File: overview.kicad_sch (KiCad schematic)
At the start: 2 parts, among them U1 SN74LVC8T245, U2 SN75160BDW

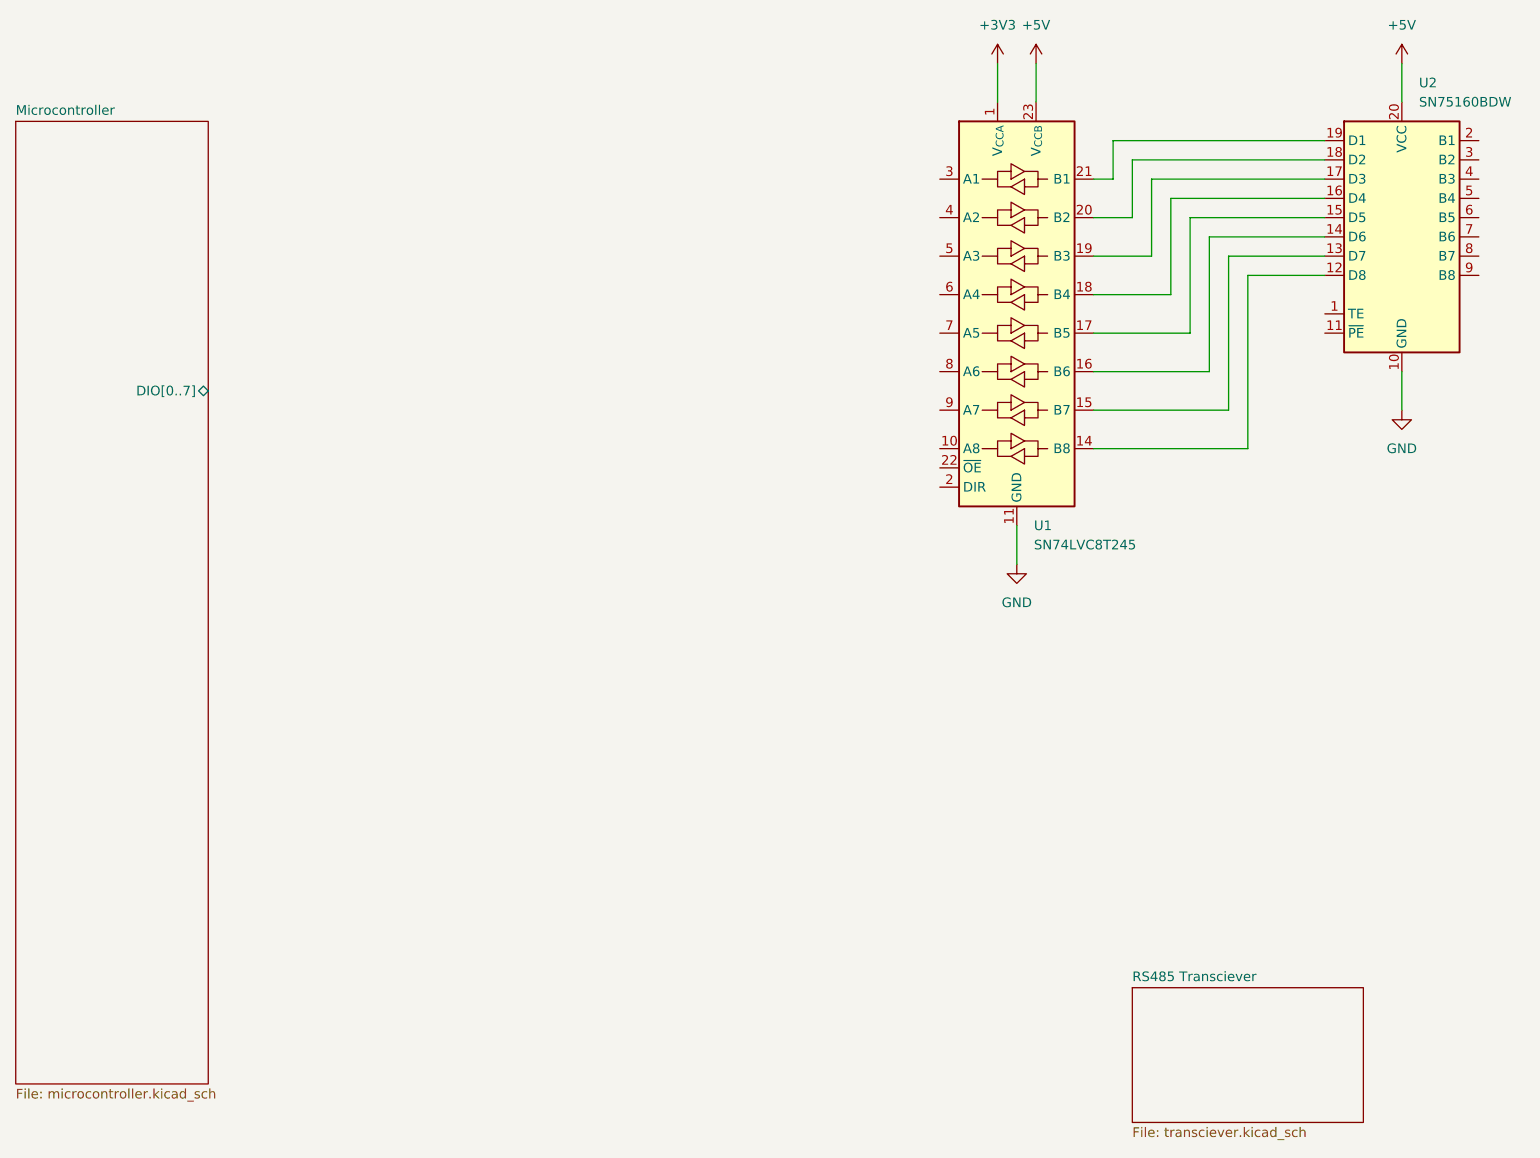
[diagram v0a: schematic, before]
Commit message: Add connectors and GPIB sub-sheets
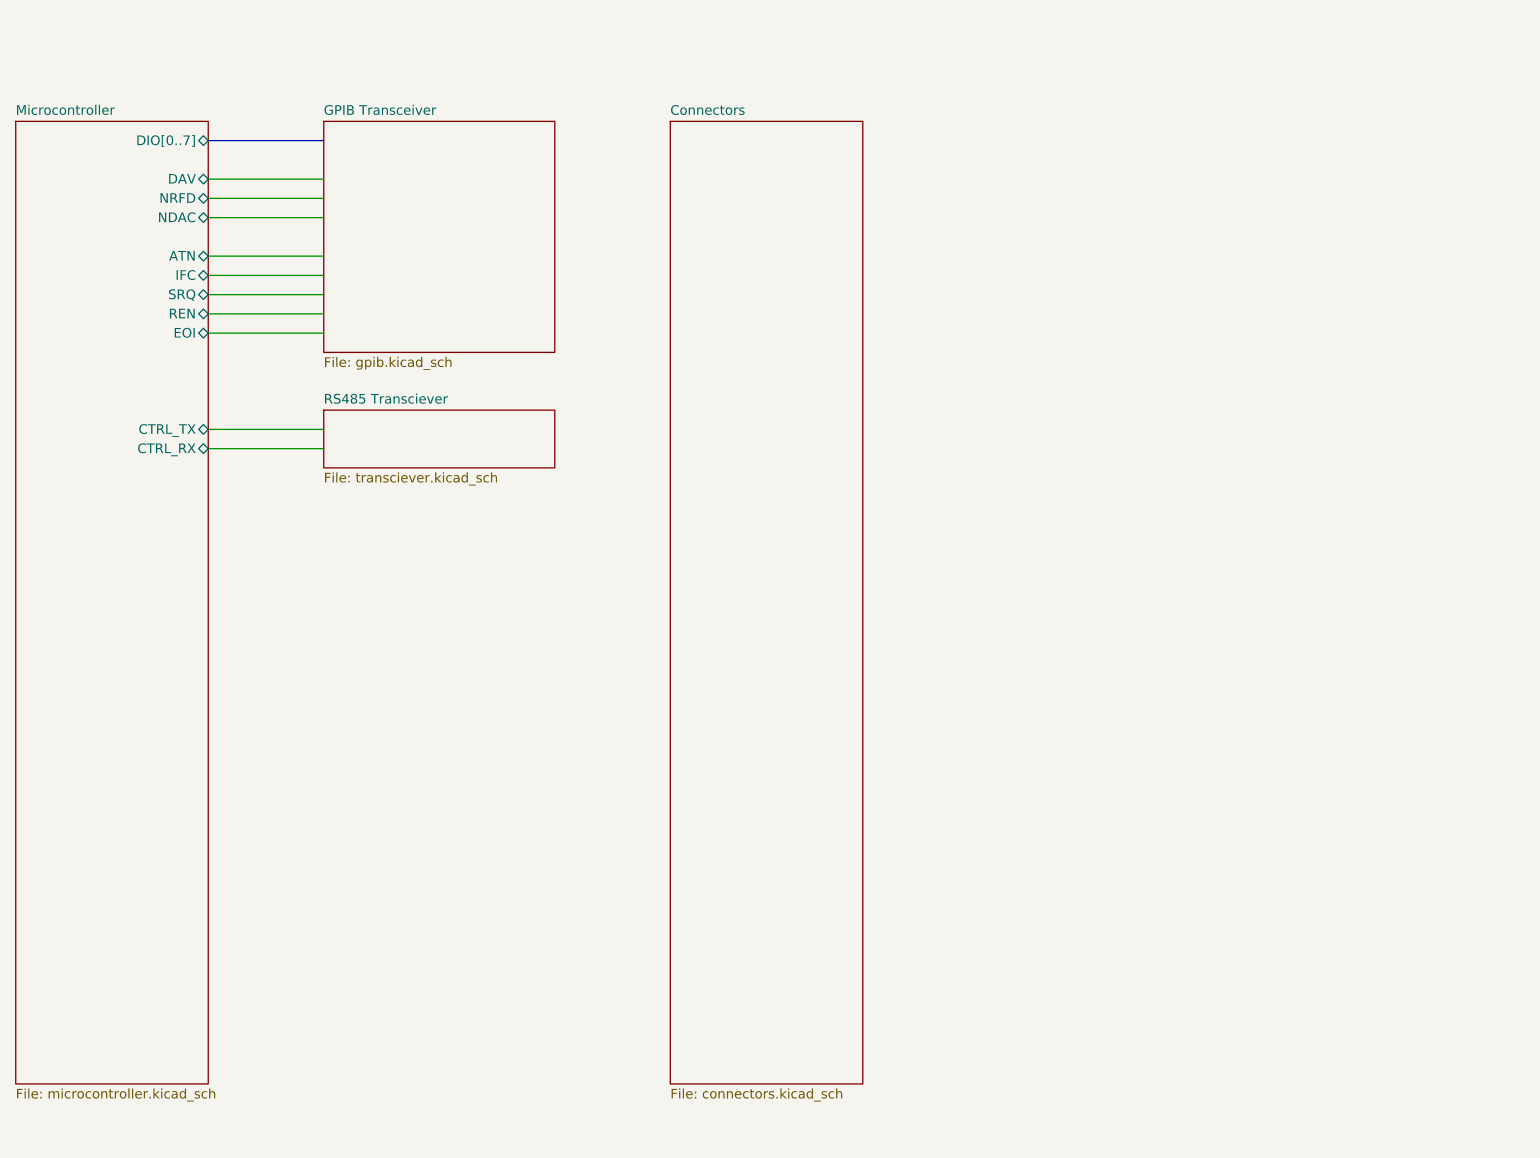
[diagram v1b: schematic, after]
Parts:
- removed U1: SN74LVC8T245, symbol Logic_LevelTranslator:SN74LVC8T245
- removed U2: SN75160BDW, Package_SO:SOIC-20W_7.5x12.8mm_P1.27mm, symbol Interface:SN75160BDW
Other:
- added sheet Connectors (connectors.kicad_sch)
- added sheet GPIB Transceiver (gpib.kicad_sch)
- sheet Microcontroller ports: added ATN, CTRL_RX, CTRL_TX, DAV, EOI, IFC, NDAC, NRFD, REN, SRQ; removed none

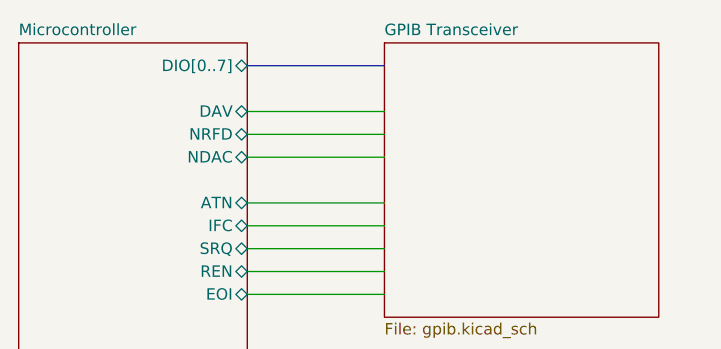
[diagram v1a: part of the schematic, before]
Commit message: Remove GPIB transcievers. Targeting modern replacements
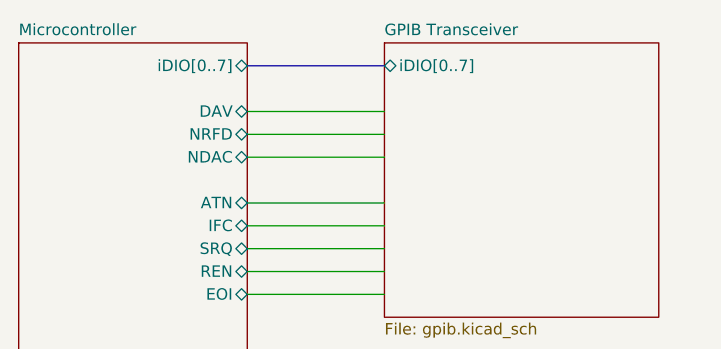
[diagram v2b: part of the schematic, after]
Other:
- sheet GPIB Transceiver ports: added iDIO[0..7]; removed none
- sheet Microcontroller ports: added iDIO[0..7]; removed DIO[0..7]
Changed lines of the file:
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@@
+			)
+		)
+		(pin "iDIO[0..7]" bidirectional
+			(at 167.64 71.12 180)
+			(effects
+				(font
+					(size 1.27 1.27)
+				)
+				(justify left)
 			)
 		)
@@
 				)
 				(justify left top)
-			)
-		)
-		(pin "DIO[0..7]" bidirectional
-			(at 152.4 71.12 0)
-			(effects
-				(font
-					(size 1.27 1.27)
-				)
-				(justify right)
 			)
 		)
@@
 			(effects
 				(font
+					(size 1.27 1.27)
+				)
+				(justify right)
+			)
+		)
+		(pin "iDIO[0..7]" bidirectional
+			(at 152.4 71.12 0)
+			(effects
+				(font

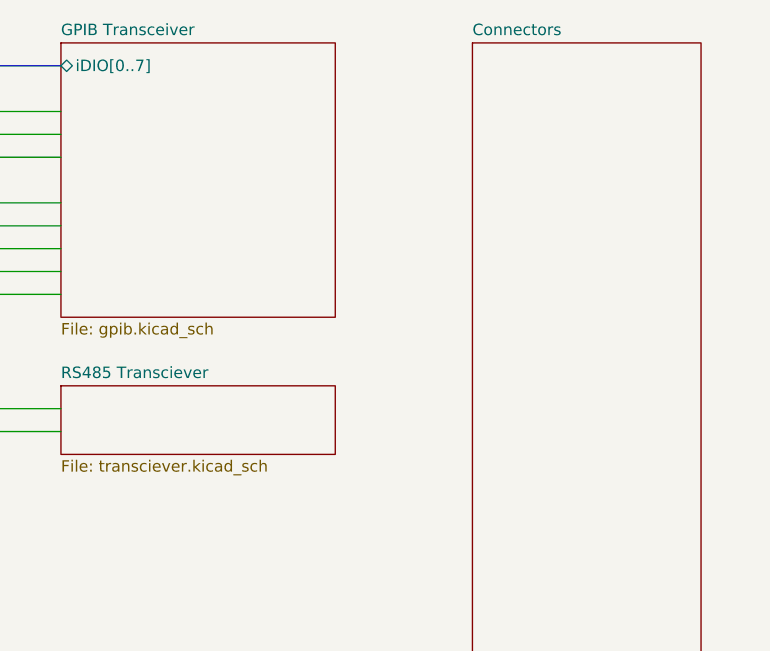
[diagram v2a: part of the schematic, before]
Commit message: Link DIO nets to GPIB connector
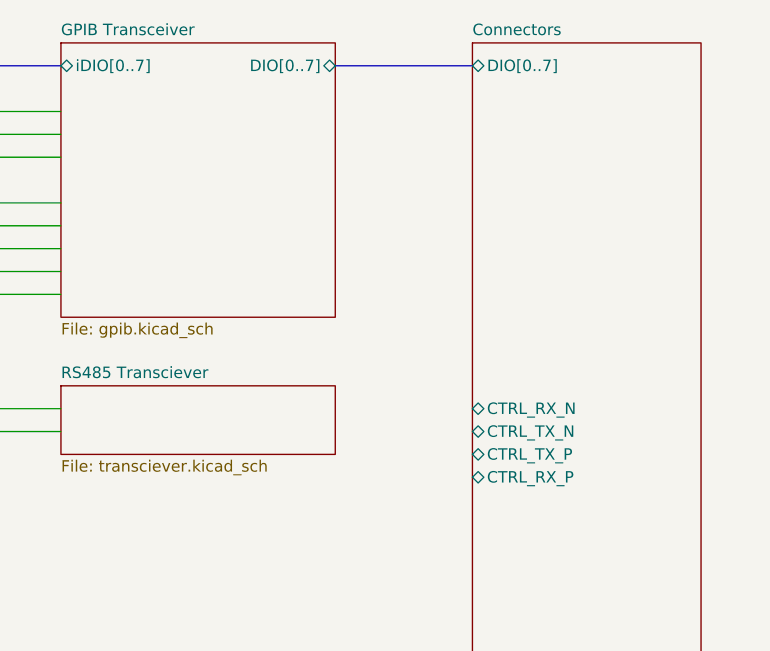
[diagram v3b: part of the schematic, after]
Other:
- sheet Connectors ports: added CTRL_RX_N, CTRL_RX_P, CTRL_TX_N, CTRL_TX_P, DIO[0..7]; removed none
- sheet GPIB Transceiver ports: added DIO[0..7]; removed none
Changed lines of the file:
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@@
+		)
+	)
+	(bus
+		(pts
+			(xy 198.12 71.12) (xy 213.36 71.12)
+		)
+		(stroke
+			(width 0)
+			(type default)
 		)
 	)
@@
 			)
 		)
+		(pin "DIO[0..7]" bidirectional
+			(at 198.12 71.12 0)
+			(effects
+				(font
+					(size 1.27 1.27)
+				)
+				(justify right)
+			)
+		)
 		(instances
 			(project "gpib_controller"
@@
 			)
 		)
+		(pin "DIO[0..7]" bidirectional
+			(at 213.36 71.12 180)
+			(effects
+				(font
+					(size 1.27 1.27)
+				)
+				(justify left)
+			)
+		)
+		(pin "CTRL_RX_N" bidirectional
+			(at 213.36 109.22 180)
+			(effects
+				(font
+					(size 1.27 1.27)
+				)
+				(justify left)
+			)
+		)
+		(pin "CTRL_TX_N" bidirectional
+			(at 213.36 111.76 180)
+			(effects
+				(font
+					(size 1.27 1.27)
+				)
+				(justify left)
+			)
+		)
+		(pin "CTRL_TX_P" bidirectional
+			(at 213.36 114.3 180)
+			(effects
+				(font
+					(size 1.27 1.27)
+				)
+				(justify left)
+			)
+		)
+		(pin "CTRL_RX_P" bidirectional
+			(at 213.36 116.84 180)
+			(effects
+				(font
+					(size 1.27 1.27)
+				)
+				(justify left)
+			)
+		)

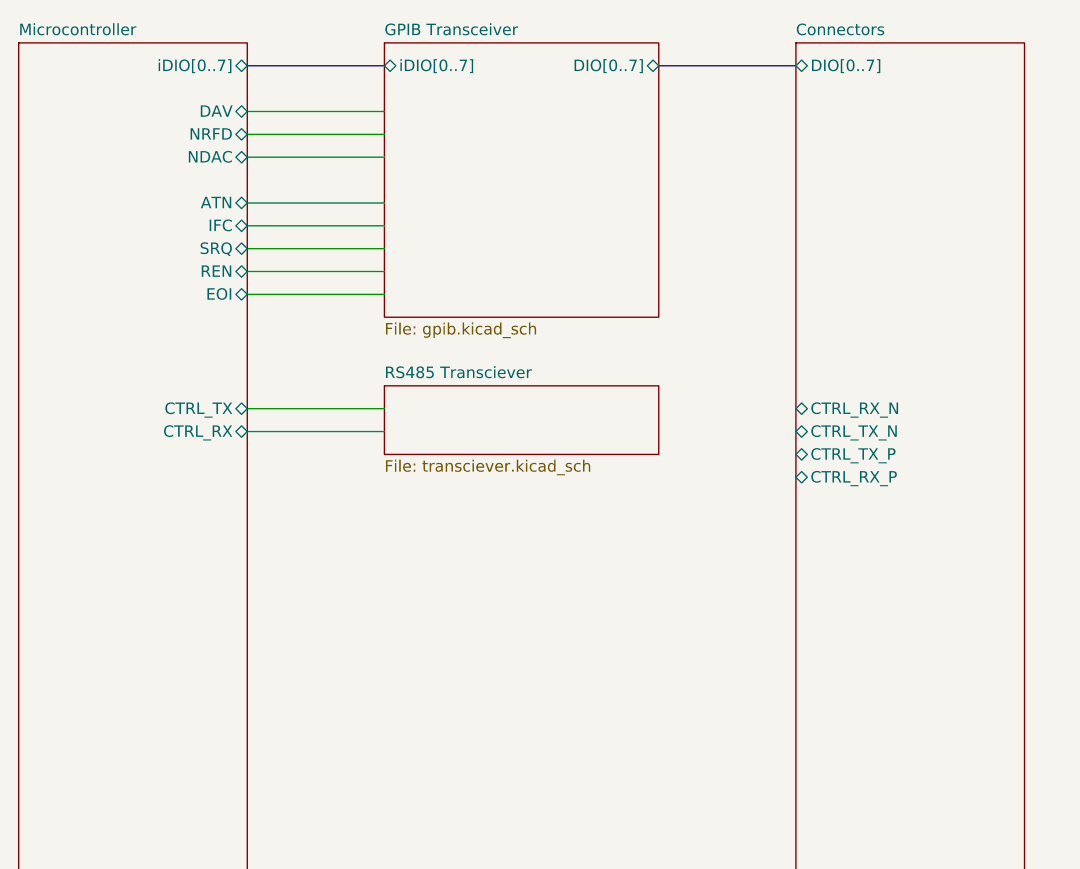
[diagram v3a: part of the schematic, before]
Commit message: Added open-drain driver for GPIB control pins
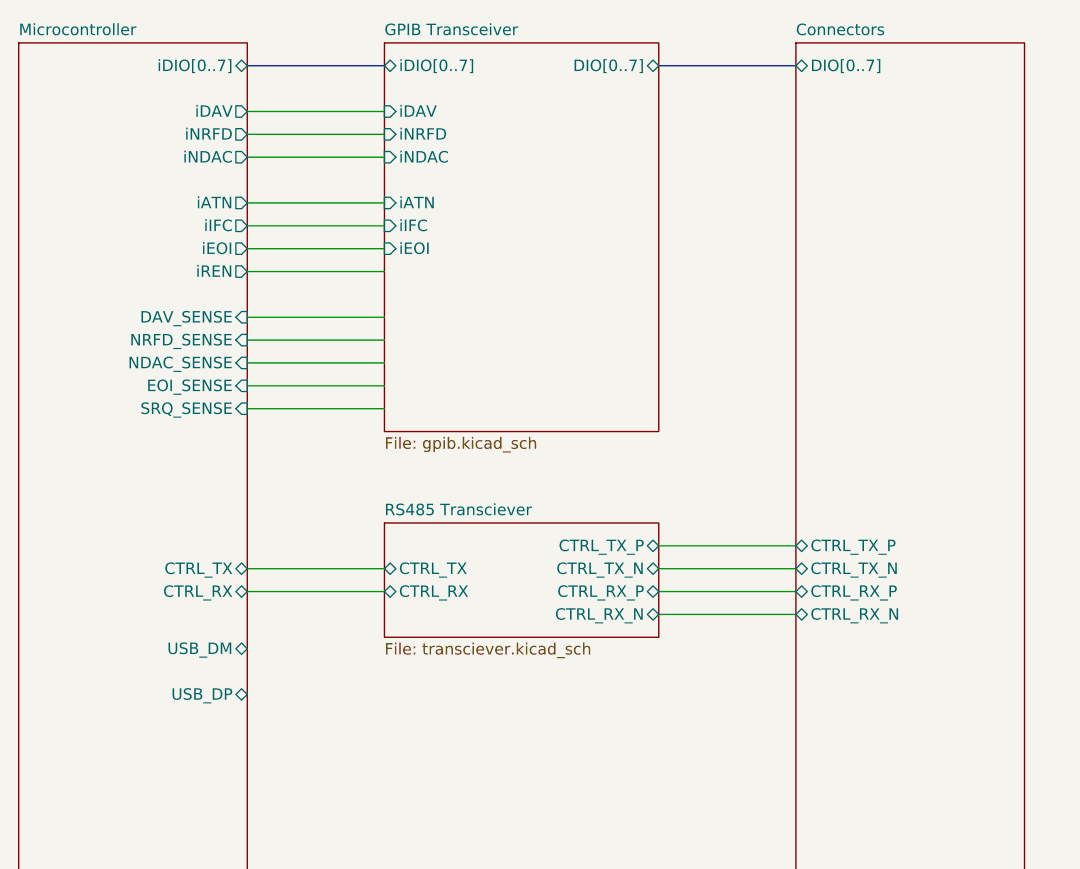
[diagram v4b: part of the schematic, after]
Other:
- sheet GPIB Transceiver ports: added iATN, iDAV, iEOI, iIFC, iNDAC, iNRFD; removed none
- sheet Microcontroller ports: added DAV_SENSE, EOI_SENSE, NDAC_SENSE, NRFD_SENSE, SRQ_SENSE, USB_DM, USB_DP, iATN, iDAV, iEOI, iIFC, iNDAC, iNRFD, iREN; removed ATN, DAV, EOI, IFC, NDAC, NRFD, REN, SRQ
- sheet RS485 Transciever ports: added CTRL_RX, CTRL_RX_N, CTRL_RX_P, CTRL_TX, CTRL_TX_N, CTRL_TX_P; removed none

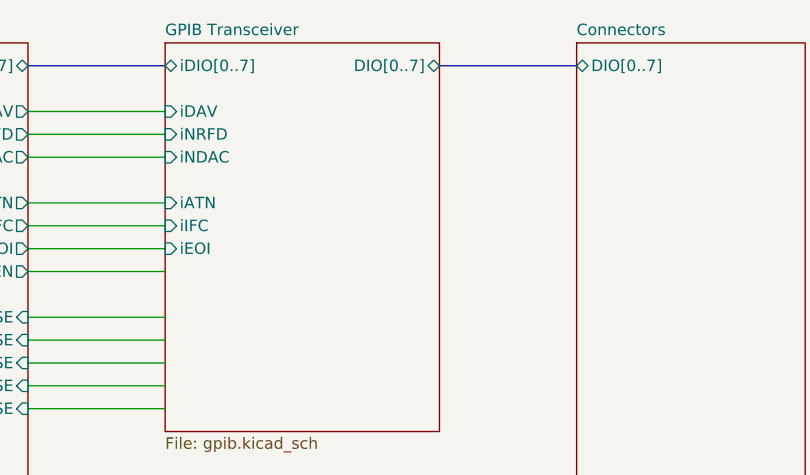
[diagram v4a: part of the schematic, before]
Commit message: Add Schmitt-Trig sense IC, connect GPIB conn nets and run jobfile
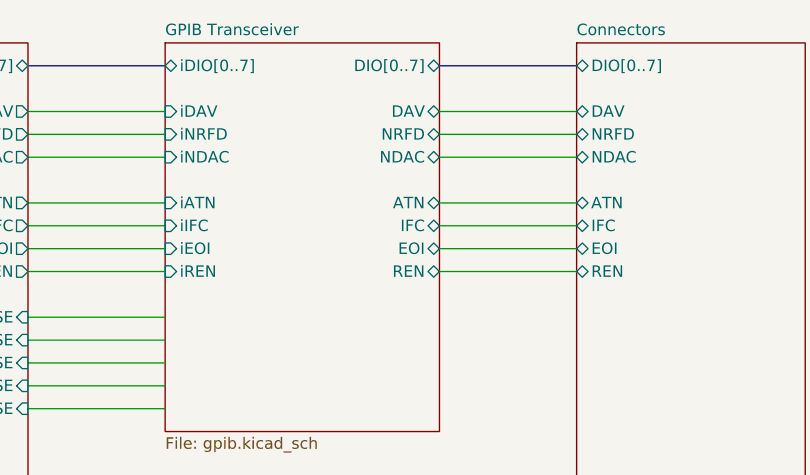
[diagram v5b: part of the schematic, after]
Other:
- sheet Connectors ports: added ATN, DAV, EOI, IFC, NDAC, NRFD, REN; removed none
- sheet GPIB Transceiver ports: added ATN, DAV, EOI, IFC, NDAC, NRFD, REN, iREN; removed none
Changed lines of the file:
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@@
+	(wire
+		(pts
+			(xy 198.12 78.74) (xy 213.36 78.74)
+		)
+		(stroke
+			(width 0)
+			(type default)
+		)
+	)
 	(wire
 		(pts
@@
 	(wire
 		(pts
+			(xy 198.12 88.9) (xy 213.36 88.9)
+		)
+		(stroke
+			(width 0)
+			(type default)
+		)
+	)
+	(wire
+		(pts
 			(xy 198.12 129.54) (xy 213.36 129.54)
 		)
@@
 	(wire
 		(pts
+			(xy 198.12 81.28) (xy 213.36 81.28)
+		)
+		(stroke
+			(width 0)
+			(type default)
+		)
+	)
+	(wire
+		(pts
 			(xy 152.4 127) (xy 167.64 127)
 		)
@@
 	(wire
 		(pts
+			(xy 198.12 86.36) (xy 213.36 86.36)
+		)
+		(stroke
+			(width 0)
+			(type default)
+		)
+	)
+	(wire
+		(pts
 			(xy 198.12 124.46) (xy 213.36 124.46)
 		)
@@
 		)
 	)
+	(wire
+		(pts
+			(xy 198.12 91.44) (xy 213.36 91.44)
+		)
+		(stroke
+			(width 0)
+			(type default)
+		)
+	)
 	(bus
 		(pts
@@
 		)
 	)
+	(wire
+		(pts
+			(xy 198.12 93.98) (xy 213.36 93.98)
+		)
+		(stroke
+			(width 0)
+			(type default)
+		)
+	)
 	(bus
 		(pts
 			(xy 152.4 71.12) (xy 167.64 71.12)
+		)
+		(stroke
+			(width 0)
+			(type default)
+		)
+	)
+	(wire
+		(pts
+			(xy 198.12 76.2) (xy 213.36 76.2)
 		)
 		(stroke
@@
 			)
 		)
+		(pin "iREN" input
+			(at 167.64 93.98 180)
+			(effects
+				(font
+					(size 1.27 1.27)
+				)
+				(justify left)
+			)
+		)
+		(pin "EOI" bidirectional
+			(at 198.12 91.44 0)
+			(effects
+				(font
+					(size 1.27 1.27)
+				)
+				(justify right)
+			)
+		)
+		(pin "REN" bidirectional
+			(at 198.12 93.98 0)
+			(effects
+				(font
+					(size 1.27 1.27)
+				)
+				(justify right)
+			)
+		)
+		(pin "DAV" bidirectional
+			(at 198.12 76.2 0)
+			(effects
+				(font
+					(size 1.27 1.27)
+				)
+				(justify right)
+			)
+		)
+		(pin "NRFD" bidirectional
+			(at 198.12 78.74 0)
+			(effects
+				(font
+					(size 1.27 1.27)
+				)
+				(justify right)
+			)
+		)
+		(pin "IFC" bidirectional
+			(at 198.12 88.9 0)
+			(effects
+				(font
+					(size 1.27 1.27)
+				)
+				(justify right)
+			)
+		)
+		(pin "ATN" bidirectional
+			(at 198.12 86.36 0)
+			(effects
+				(font
+					(size 1.27 1.27)
+				)
+				(justify right)
+			)
+		)
+		(pin "NDAC" bidirectional
+			(at 198.12 81.28 0)
+			(effects
+				(font
+					(size 1.27 1.27)
+				)
+				(justify right)
+			)
+		)
 		(instances
 			(project "gpib_controller"
@@
 			(effects
 				(font
+					(size 1.27 1.27)
+				)
+				(justify left)
+			)
+		)
+		(pin "REN" bidirectional
+			(at 213.36 93.98 180)
+			(effects
+				(font
+					(size 1.27 1.27)
+				)
+				(justify left)
+			)
+		)
+		(pin "NDAC" bidirectional
+			(at 213.36 81.28 180)
+			(effects
+				(font
+					(size 1.27 1.27)
+				)
+				(justify left)
+			)
+		)
+		(pin "EOI" bidirectional
+			(at 213.36 91.44 180)
+			(effects
+				(font
+					(size 1.27 1.27)
+				)
+				(justify left)
+			)
+		)
+		(pin "ATN" bidirectional
+			(at 213.36 86.36 180)
+			(effects
+				(font
+					(size 1.27 1.27)
+				)
+				(justify left)
+			)
+		)
+		(pin "DAV" bidirectional
+			(at 213.36 76.2 180)
+			(effects
+				(font
+					(size 1.27 1.27)
+				)
+				(justify left)
+			)
+		)
+		(pin "IFC" bidirectional
+			(at 213.36 88.9 180)
+			(effects
+				(font
+					(size 1.27 1.27)
+				)
+				(justify left)
+			)
+		)
+		(pin "NRFD" bidirectional
+			(at 213.36 78.74 180)
+			(effects
+				(font
